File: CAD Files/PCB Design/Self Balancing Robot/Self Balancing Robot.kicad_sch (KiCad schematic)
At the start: 14 parts, among them J1 Screw_Terminal_01x02, M1 Stepper_Motor_bipolar, M2 Stepper_Motor_bipolar, U1 DEVKIT_V1_ESP32-WROOM-32, U2 TSR_1-2450

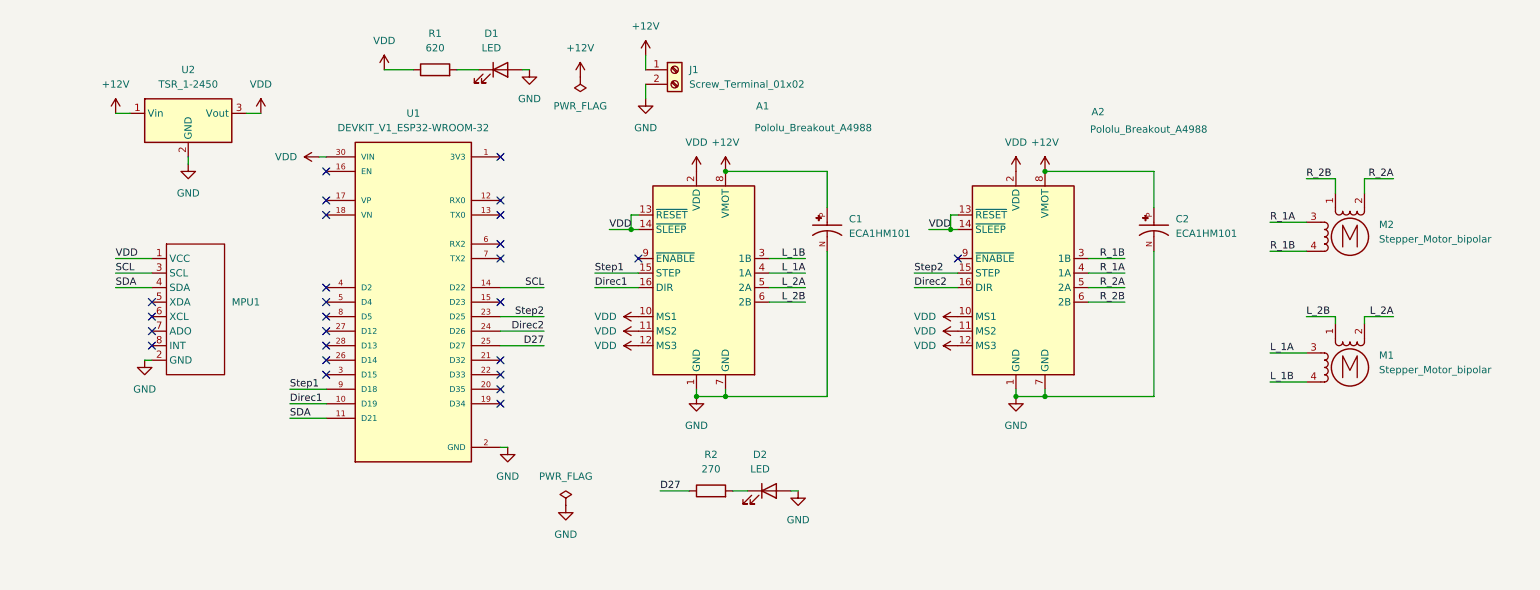
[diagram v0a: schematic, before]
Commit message: Added decoupling capacitors to ESP32, MPU, VDD, and 12V rails. Replaced screw terminal with XT60 female connector. Changed GPIO pins used for steppers and LED for optimal layout. Step1: GPIO19  Direc1: D18 Step2: GPIO5 Direc2: 17 DiagLED: GPIO36
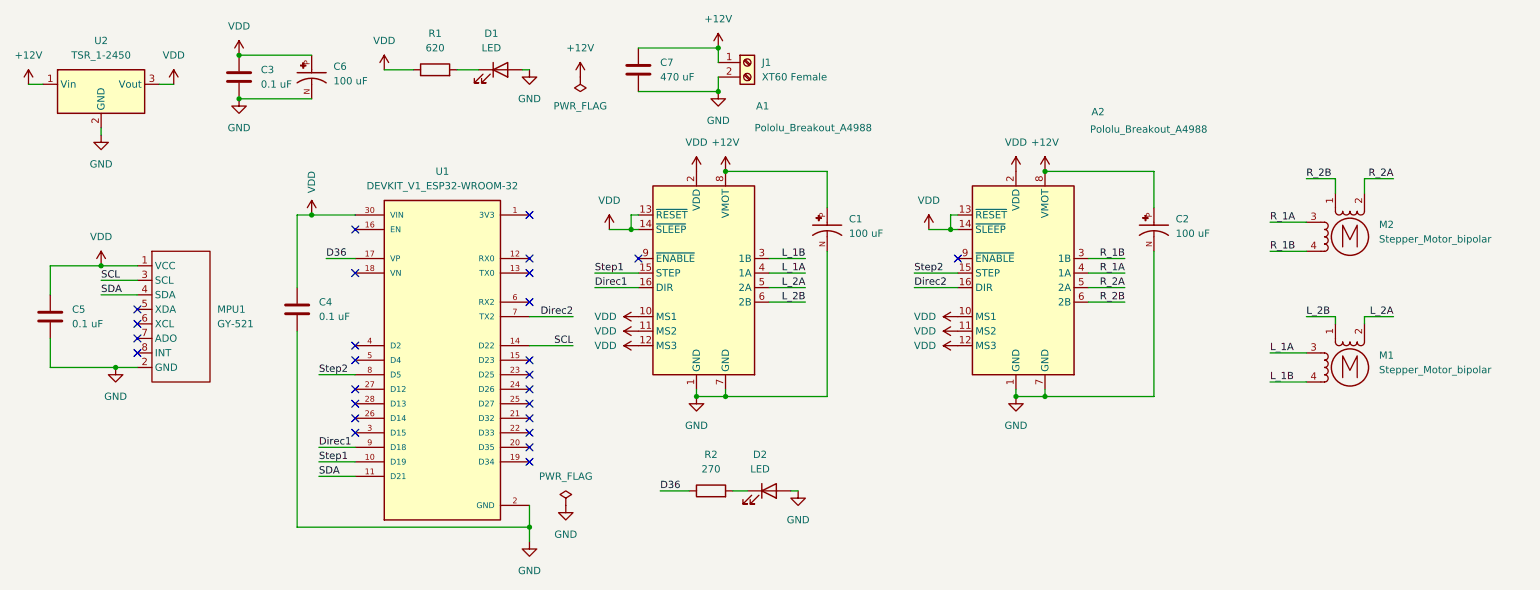
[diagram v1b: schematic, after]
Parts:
- added C3, C4, C5: 0.1 uF, Capacitor_SMD:C_0805_2012Metric_Pad1.18x1.45mm_HandSolder, symbol Device:C
- added C6: 100 uF, TW Footprints:CP_Radial_D6.3mm_P2.50mm, symbol TW_Symbols:ECA1HM101
- added C7: 470 uF, Capacitor_THT:CP_Radial_D10.0mm_P5.00mm, symbol Device:C
- C1, C2: value ECA1HM101 -> 100 uF
- J1: value Screw_Terminal_01x02 -> XT60 Female; footprint TerminalBlock:TerminalBlock_MaiXu_MX126-5.0-02P_1x02_P5.00mm -> Connector_AMASS:AMASS_XT60-F_1x02_P7.20mm_Vertical
- MPU1: value ~ -> GY-521
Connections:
- net +12V: now also C7.1
- net Direc1: now also U1.9 (D18); no longer U1.10 (D19)
- net Direc2: now also U1.7 (TX2); no longer U1.24 (D26)
- net GND: now also C3.2, C4.2, C5.2, C6.N, C7.2
- net Step1: now also U1.10 (D19); no longer U1.9 (D18)
- net Step2: now also U1.8 (D5); no longer U1.23 (D25)
- net VDD: now also C3.1, C4.1, C5.1, C6.P
- net D36: now reaches U1.17 (VP)
- net D36: now also R2.1
- net D27: no longer names the net of U1.25 (D27)
- net D27: no longer R2.1
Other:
- moved on the sheet: J1, MPU1, U1, U2

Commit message: replace servo connectors from JST- EH to JST-XH because more common connector type
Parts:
- M1, M2: footprint Connector_JST:JST_EH_S4B-EH_1x04_P2.50mm_Horizontal -> Connector_JST:JST_XH_S4B-XH-A_1x04_P2.50mm_Horizontal
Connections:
- net L_1A: now also M1.2 (-); no longer M1.3
- net L_1B: now also M1.1; no longer M1.4
- net L_2A: now also M1.3; no longer M1.2 (-)
- net L_2B: now also M1.4; no longer M1.1
- net R_1A: now also M2.2 (-); no longer M2.3
- net R_1B: now also M2.1; no longer M2.4
- net R_2A: now also M2.3; no longer M2.2 (-)
- net R_2B: now also M2.4; no longer M2.1
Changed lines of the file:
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@@
 	)
 	(label "R_2B"
-		(at 246.38 41.91 0)
+		(at 240.03 54.61 0)
 		(effects
 			(font
@@
 	)
 	(label "R_2A"
-		(at 261.62 41.91 180)
+		(at 240.03 49.53 0)
 		(effects
 			(font
 				(size 1.27 1.27)
 			)
-			(justify right bottom)
+			(justify left bottom)
 		)
 	)
 	(label "L_2B"
-		(at 246.38 66.04 0)
+		(at 240.03 77.47 0)
 		(effects
 			(font
@@
 	)
 	(label "R_1A"
-		(at 240.03 49.53 0)
+		(at 261.62 41.91 180)
 		(effects
 			(font
 				(size 1.27 1.27)
 			)
-			(justify left bottom)
+			(justify right bottom)
 		)
 	)
 	(label "L_1A"
-		(at 240.03 72.39 0)
+		(at 261.62 66.04 180)
 		(effects
 			(font
 				(size 1.27 1.27)
 			)
-			(justify left bottom)
+			(justify right bottom)
 		)
 	)
@@
 	)
 	(label "R_1B"
-		(at 240.03 54.61 0)
+		(at 246.38 41.91 0)
 		(effects
 			(font
@@
 	)
 	(label "L_1B"
-		(at 240.03 77.47 0)
+		(at 246.38 66.04 0)
 		(effects
 			(font
@@
 	)
 	(label "L_2A"
-		(at 261.62 66.04 180)
+		(at 240.03 72.39 0)
 		(effects
 			(font
 				(size 1.27 1.27)
 			)
-			(justify right bottom)
+			(justify left bottom)
 		)
 	)
@@
 			)
 		)
-		(property "Footprint" "Connector_JST:JST_EH_S4B-EH_1x04_P2.50mm_Horizontal"
+		(property "Footprint" "Connector_JST:JST_XH_S4B-XH-A_1x04_P2.50mm_Horizontal"
 			(at 254.254 75.184 0)
 			(effects
@@
 			)
 		)
-		(property "Footprint" "Connector_JST:JST_EH_S4B-EH_1x04_P2.50mm_Horizontal"
+		(property "Footprint" "Connector_JST:JST_XH_S4B-XH-A_1x04_P2.50mm_Horizontal"
 			(at 254.254 52.324 0)
 			(effects

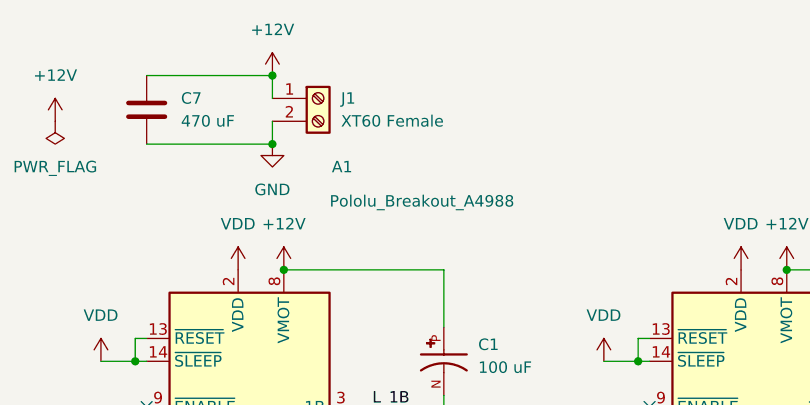
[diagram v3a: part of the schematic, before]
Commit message: Replace XT60 Female with Male header
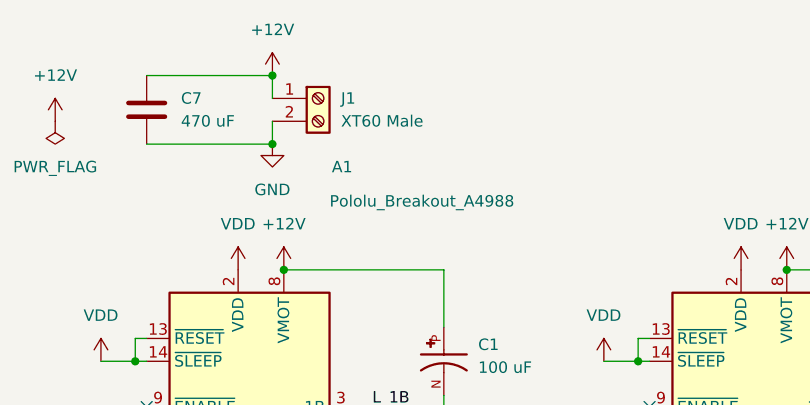
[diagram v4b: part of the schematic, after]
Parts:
- J1: value XT60 Female -> XT60 Male; footprint Connector_AMASS:AMASS_XT60-F_1x02_P7.20mm_Vertical -> Connector_AMASS:AMASS_XT60-M_1x02_P7.20mm_Vertical
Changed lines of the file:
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@@
 			)
 		)
-		(property "Value" "XT60 Female"
+		(property "Value" "XT60 Male"
 			(at 151.13 24.1299 0)
 			(effects
@@
 			)
 		)
-		(property "Footprint" "Connector_AMASS:AMASS_XT60-F_1x02_P7.20mm_Vertical"
+		(property "Footprint" "Connector_AMASS:AMASS_XT60-M_1x02_P7.20mm_Vertical"
 			(at 148.59 21.59 0)
 			(effects
